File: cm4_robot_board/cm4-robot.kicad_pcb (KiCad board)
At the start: 4 copper layers, 118 x 117 mm, 263 parts, among them J1 1747981-1, J10 Conn_01x04, J11 Conn_01x03, J12 Conn_01x04, J13 M12A-08PFFR-SF7003, J14 Power Sw, J15 I2C OLED, J18 Serial Rear, J19 SBUS, J2 M12A-08PFFR-SF7003, J21 Conn_01x03, J22 DNP, J23 Conn_01x01, J24 Conn_01x01, J25 RJ45, J3 USB_C_Receptacle_USB2.0, J4 Conn_01x04, J5 Conn_01x04, J6 Conn_01x04, J7 USB_A, J8 Conn_01x02, J9 ESTOP, Q1 Q_PMOS_GSD, Q10 Q_NMOS_GSD, Q2 Q_NMOS_GSD, Q3 Q_NMOS_GSD, Q4 Q_NMOS_GSD, Q5 Q_NMOS_GSD, Q6 AO3401A, Q7 AO3400A, Q8 Si2328DS, Q9 AO3401A, SW1 B3U-1000P, SW2 SW_SPDT, SW3 SW_SPDT, SW4 SW_SPDT, SW5 SW_SPDT, SW6 SW_DIP_x02, SW7 CONFIG_SW, U1 SN74LVC1G07QDCKTQ1, U10 isolator, U11 isolator, U12 TPS61040DBVR, U13 SC16IS752, U14 SC16IS752, U15 SN74LVC1G07QDCKTQ1, U16 CC56-12SEKWA, U17 ET6226M, U18 SN74LVC1G07QDCKTQ1, U19 SN74LVC1G07QDCKTQ1, U2 SN74LVC1G07QDCKTQ1, U20 TLV1117LV33DCYR, U21 FT231XS, U22 SN74LVC1G07QDCKTQ1, U23 TPD4E1U06DCKR, U24 ISL54222AIUZ, U25 USBLC6-2P6, U26 USBLC6-2P6, U27 SN74LVC1G07QDCKTQ1, U28 PCA9536D, U29 SN74LVC1G07QDCKTQ1, U3 LM2576HVS-5, U30 SN74LVC1G07QDCKTQ1, U31 LSM6DS3, U32 LIS3MDL, U33 ADS1115IDGS, U34 SN74LVC1G07QDCKTQ1, U35 SN74LVC1G07QDCKTQ1, U36 SN74LVC1G07QDCKTQ1, U4 TPD4E1U06DCKR, U5 ISL54222AIUZ, U6 LTC4412xS6, U7 TXS0101DCKR, U8 MCP2515-xSO, U9 MCP2515-xSO, Y1 16MHz, Y2 16MHz, Y3 14.7456MHz, Y4 14.7456MHz

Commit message: Resolve most of the schematic ERC errors.
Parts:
- C53: value 100n -> 0.1u

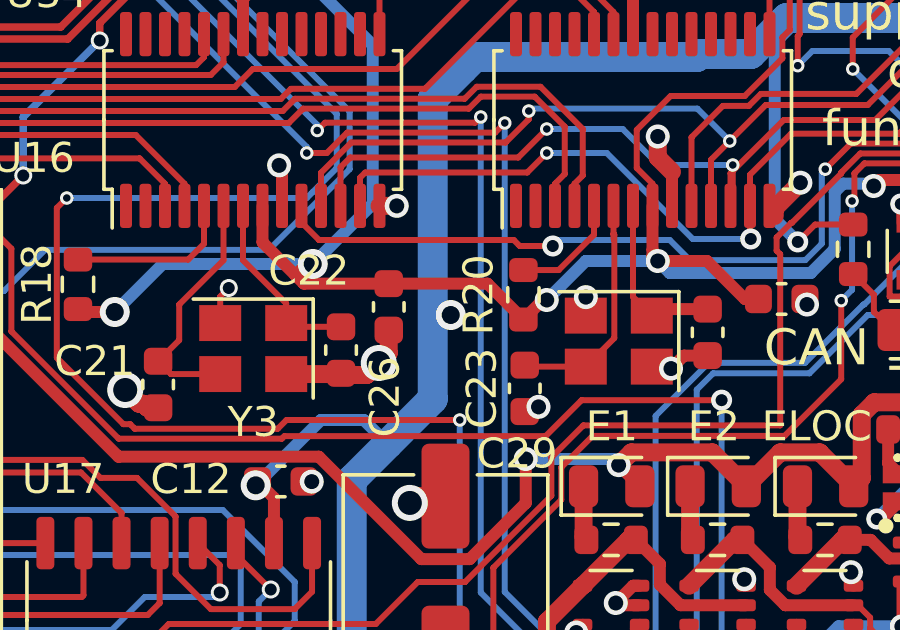
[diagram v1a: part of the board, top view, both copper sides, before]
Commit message: Clean up additional ERC warnings.
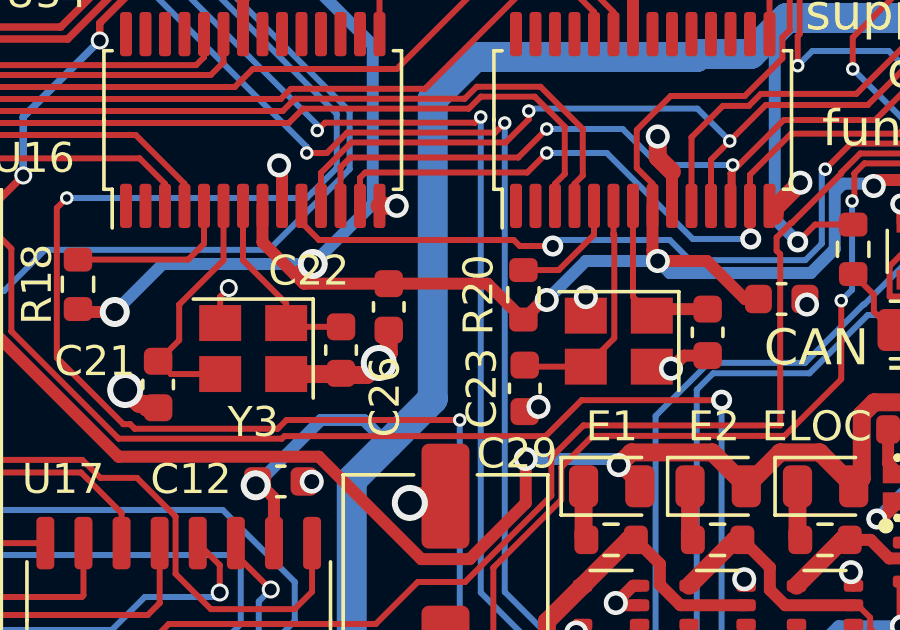
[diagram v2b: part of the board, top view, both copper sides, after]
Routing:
- net +3V3: track 734.3 -> 734.0 mm, vias 38 -> 37
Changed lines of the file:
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@@
-	)
-	(via
-		(at 107.6 113)
-		(size 1)
-		(drill 0.6)
-		(layers "F.Cu" "B.Cu")
-		(net 2)
 	)
 	(via
@@
 		(layer "B.Cu")
 		(net 2)
-	)
-	(segment
-		(start 107.25 113)
-		(end 107.6 113)
-		(width 0.4)
-		(layer "B.Cu")
-		(net 2)

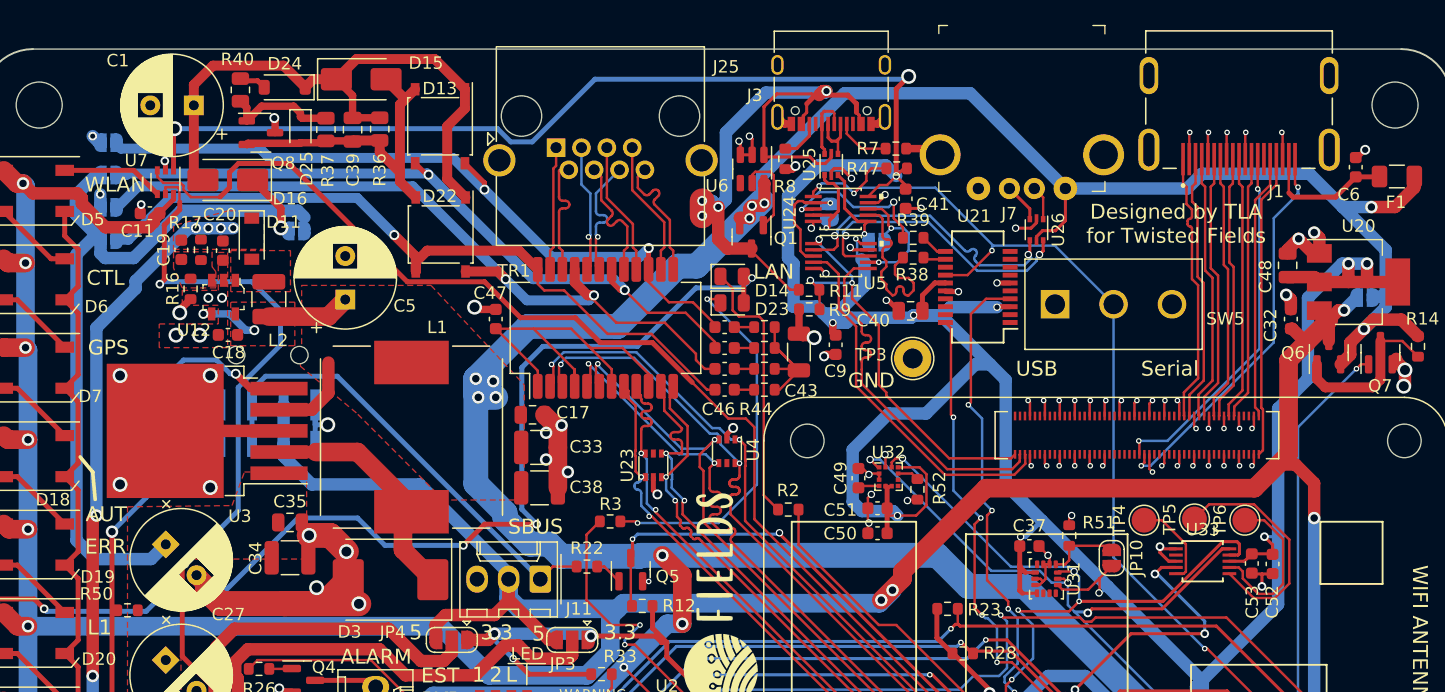
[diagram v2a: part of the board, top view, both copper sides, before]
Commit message: Update with most design review feedback. Needs final checkout.
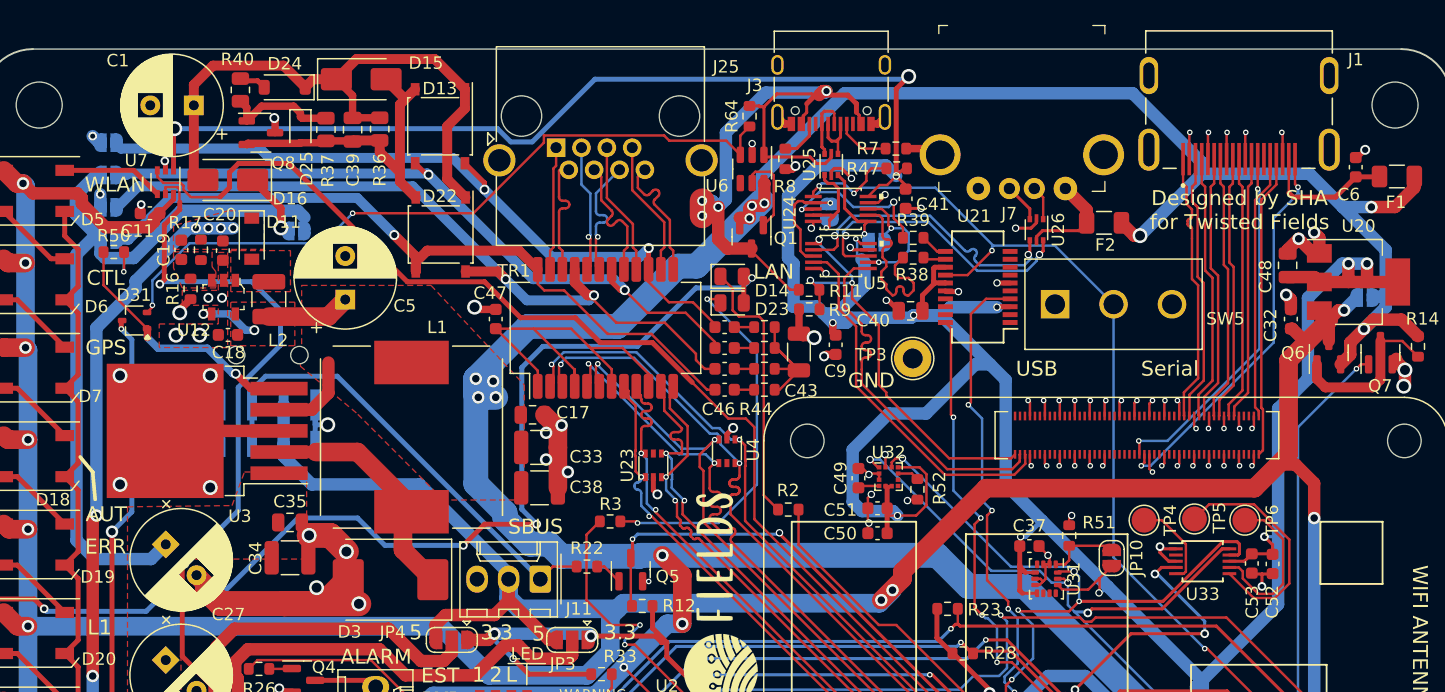
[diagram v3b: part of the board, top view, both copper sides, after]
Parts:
- added D31: Diode Dual Common Cathode 80v maximum reverse voltage, Package_TO_SOT_SMD:SOT-323_SC-70, F.Cu at (52.2, 51.8)
- added F2: Polyfuse, Fuse:Fuse_1206_3216Metric, F.Cu at (130.1, 44.0)
- added R64: 10K, Resistor_SMD:R_0603_1608Metric, F.Cu at (101.6, 35.4)
- C10, C4, C7, C8: value 18p -> 18pF 50V
- C11, C12, C13, C14, C15, C16, C25, C26, C30, C31, C36, C37, C40, C41, C47, C49, C50, C6, C9: value 0.1uF -> 0.1uF 50V
- C17, C48: value 10u -> 10uF 25V
- C18: value 4.7uF -> 4.7uF 25V
- C19: value 22pF -> 22pF 50V
- C2, C3: value 10uF -> 10uF 25V
- C20: value 1uF -> 1uF 25V
- C21, C22, C23, C24: value 22p -> 22pF 50V
- C32, C51, C52: value 1u -> 1uF 50V
- C39: value 0.1uF -> 0.1uF 100V
- C53: value 0.1u -> 0.1uF 50V
- R12, R14, R23, R28, R29, R30, R33, R47, R48, R49, R5, R58, R6, R61, R62, R63: value 10k -> 10K
- R38, R39: value 27 -> 27R
- moved R50 28.8 mm to (50.5, 46.3)
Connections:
- J7 pad 1: +5V -> /5V_FUSED
- R50 pad 2: /~{5V_EN} -> /~{VIN_5V_EN}
- U21 pad 13: unconnected-(U21-3V3OUT-Pad13) -> +3V3
- U26 pad 5: +5V -> /5V_FUSED
- U3 pad 5: /~{5V_EN} -> /~{VIN_5V_EN}
- U6 pad 3: GND -> /~{VBUS_5V_ENA}
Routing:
- net /~{VBUS_5V_ENA}: track 0.00 -> 58.4 mm, vias 0 -> 2
- net /~{VIN_5V_EN}: track 0.00 -> 20.6 mm, vias 0 -> 2
- net /5V_FUSED: track 0.00 -> 8.32 mm
- net /~{5V_EN}: track 177.3 -> 170.5 mm
- net GND: track 295.5 -> 292.7 mm, vias 174 -> 173
- net VMOT: track 76.7 -> 79.5 mm, vias 0 -> 1
- net +5V: track 423.2 -> 425.9 mm, vias 21 -> 22
- net +3V3: track 734.0 -> 736.2 mm
- net USBC_VBUS_IN: track 56.0 -> 57.2 mm
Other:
- board text added: "Designed by SHA for Twisted Fields"
- board text removed: "Designed by TLA for Twisted Fields"
